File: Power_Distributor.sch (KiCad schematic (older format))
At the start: 1 part, among them J1 Thruster_Off_Switch

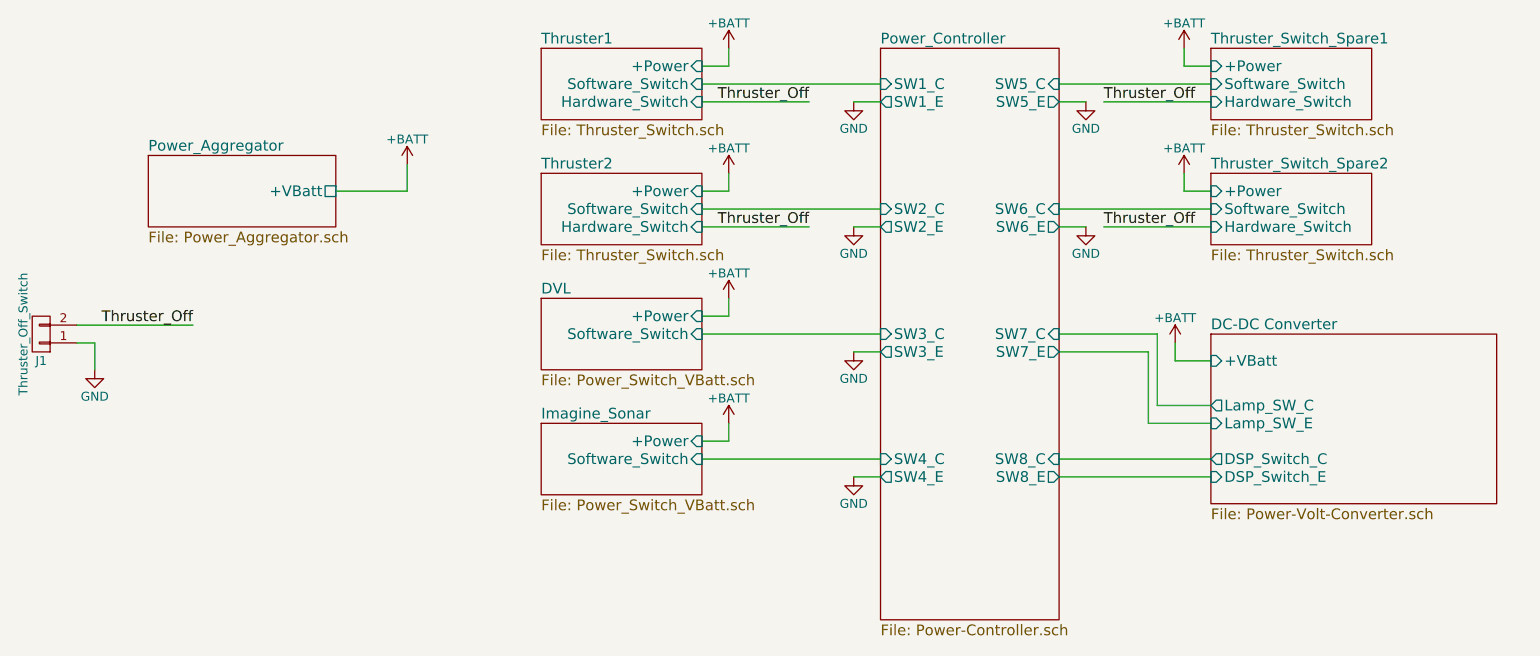
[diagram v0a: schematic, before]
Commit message: Fixed bugs from misunderstanding about Thruster, DVL, and Sonar switch biases.
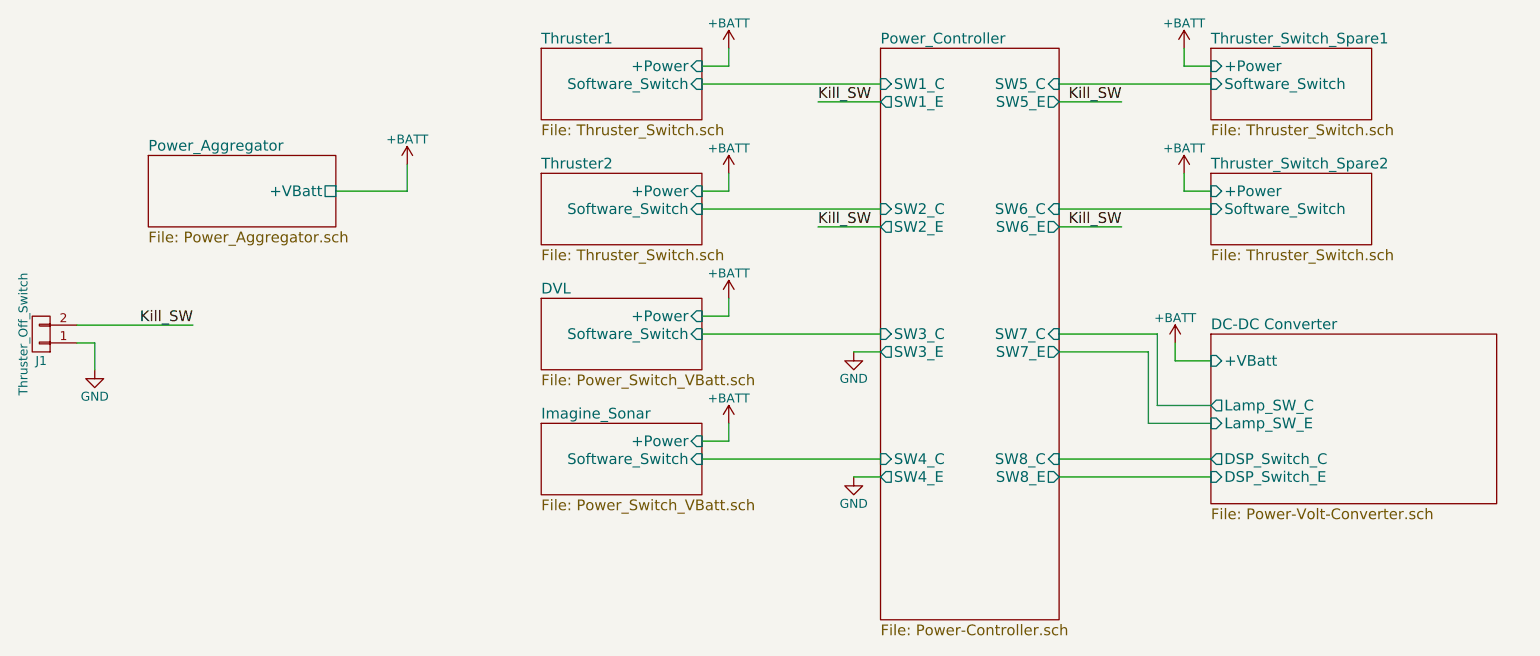
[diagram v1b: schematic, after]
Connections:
- net Thruster_Off renamed Kill_SW
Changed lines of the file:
@@
 F2 "+Power" I R 5450 3350 60
 F3 "Software_Switch" I R 5450 3450 60
-F4 "Hardware_Switch" I R 5450 3550 60
 $EndSheet
 $Sheet
@@
 F2 "+Power" I L 8300 2650 60
 F3 "Software_Switch" I L 8300 2750 60
-F4 "Hardware_Switch" I L 8300 2850 60
 $EndSheet
 $Sheet
@@
 F2 "+Power" I L 8300 3350 60
 F3 "Software_Switch" I L 8300 3450 60
-F4 "Hardware_Switch" I L 8300 3550 60
 $EndSheet
 $Comp
@@
 $EndComp
 Text Label 2600 4100 2    60   ~ 0
-Thruster_Off
+Kill_SW
 $Comp
 L GND #PWR1
@@
 	1    0    0    -1
 $EndComp
-Text Label 6050 2850 2    60   ~ 0
-Thruster_Off
 $Sheet
 S 4550 2550 900  400
@@
 F2 "+Power" I R 5450 2650 60
 F3 "Software_Switch" I R 5450 2750 60
-F4 "Hardware_Switch" I R 5450 2850 60
-$EndSheet
-Text Label 6050 3550 2    60   ~ 0
-Thruster_Off
+$EndSheet
 Wire Wire Line
 	1950 4200 2050 4200
@@
 Wire Wire Line
 	2600 4100 1950 4100
-Text Label 7700 2850 0    60   ~ 0
-Thruster_Off
-Wire Wire Line
-	7700 2850 8300 2850
-Wire Wire Line
-	6050 2850 5450 2850
-Wire Wire Line
-	6050 3550 5450 3550
-Text Label 7700 3550 0    60   ~ 0
-Thruster_Off
-Wire Wire Line
-	7700 3550 8300 3550
 $Comp
 L +BATT #PWR3
@@
 	5600 4750 5600 4650
 $Comp
-L +BATT #PWR14
+L +BATT #PWR10
 U 1 1 58EC0437
 P 8150 2550
-F 0 "#PWR14" H 8150 2400 50  0001 C CNN
+F 0 "#PWR10" H 8150 2400 50  0001 C CNN
 F 1 "+BATT" H 8150 2690 50  0000 C CNN
 F 2 "" H 8150 2550 50  0001 C CNN
@@
 	8150 2650 8300 2650
 $Comp
-L +BATT #PWR15
+L +BATT #PWR11
 U 1 1 58ECB208
 P 8150 3250
-F 0 "#PWR15" H 8150 3100 50  0001 C CNN
+F 0 "#PWR11" H 8150 3100 50  0001 C CNN
 F 1 "+BATT" H 8150 3390 50  0000 C CNN
 F 2 "" H 8150 3250 50  0001 C CNN
@@
 $EndSheet
 $Comp
-L +BATT #PWR13
+L +BATT #PWR9
 U 1 1 58E67F6C
 P 8100 4200
-F 0 "#PWR13" H 8100 4050 50  0001 C CNN
+F 0 "#PWR9" H 8100 4050 50  0001 C CNN
 F 1 "+BATT" H 8100 4340 50  0000 C CNN
 F 2 "" H 8100 4200 50  0001 C CNN
@@
 $Comp
 L GND #PWR7
-U 1 1 58E667A4
-P 6300 2850
-F 0 "#PWR7" H 6300 2600 50  0001 C CNN
-F 1 "GND" H 6300 2700 50  0000 C CNN
-F 2 "" H 6300 2850 50  0001 C CNN
-F 3 "" H 6300 2850 50  0001 C CNN
-	1    6300 2850
-	1    0    0    -1
-$EndComp
-$Comp
-L GND #PWR8
-U 1 1 58E66896
-P 6300 3550
-F 0 "#PWR8" H 6300 3300 50  0001 C CNN
-F 1 "GND" H 6300 3400 50  0000 C CNN
-F 2 "" H 6300 3550 50  0001 C CNN
-F 3 "" H 6300 3550 50  0001 C CNN
-	1    6300 3550
-	1    0    0    -1
-$EndComp
-$Comp
-L GND #PWR9
 U 1 1 58E66A79
 P 6300 4250
-F 0 "#PWR9" H 6300 4000 50  0001 C CNN
+F 0 "#PWR7" H 6300 4000 50  0001 C CNN
 F 1 "GND" H 6300 4100 50  0000 C CNN
 F 2 "" H 6300 4250 50  0001 C CNN
@@
 $EndComp
 $Comp
-L GND #PWR10
+L GND #PWR8
 U 1 1 58E66B6B
 P 6300 4950
-F 0 "#PWR10" H 6300 4700 50  0001 C CNN
+F 0 "#PWR8" H 6300 4700 50  0001 C CNN
 F 1 "GND" H 6300 4800 50  0000 C CNN
 F 2 "" H 6300 4950 50  0001 C CNN
@@
 	1    0    0    -1
 $EndComp
-$Comp
-L GND #PWR12
-U 1 1 58E66C5D
-P 7600 3550
-F 0 "#PWR12" H 7600 3300 50  0001 C CNN
-F 1 "GND" H 7600 3400 50  0000 C CNN
-F 2 "" H 7600 3550 50  0001 C CNN
-F 3 "" H 7600 3550 50  0001 C CNN
-	1    7600 3550
-	1    0    0    -1
-$EndComp
-$Comp
-L GND #PWR11
-U 1 1 58E66D4F
-P 7600 2850
-F 0 "#PWR11" H 7600 2600 50  0001 C CNN
-F 1 "GND" H 7600 2700 50  0000 C CNN
-F 2 "" H 7600 2850 50  0001 C CNN
-F 3 "" H 7600 2850 50  0001 C CNN
-	1    7600 2850
-	1    0    0    -1
-$EndComp
-Wire Wire Line
-	6450 2850 6300 2850
-Wire Wire Line
-	6450 3550 6300 3550
+Wire Wire Line
+	6100 2850 6450 2850
+Wire Wire Line
+	6100 3550 6450 3550
 Wire Wire Line
 	6300 4250 6450 4250
@@
 	6450 4950 6300 4950
 Wire Wire Line
-	7450 3550 7600 3550
-Wire Wire Line
-	7450 2850 7600 2850
+	7450 3550 7800 3550
+Wire Wire Line
+	7450 2850 7800 2850
+Text Label 6100 2850 0    60   ~ 0
+Kill_SW
+Text Label 6100 3550 0    60   ~ 0
+Kill_SW
+Text Label 7800 2850 2    60   ~ 0
+Kill_SW
+Text Label 7800 3550 2    60   ~ 0
+Kill_SW
 $EndSCHEMATC

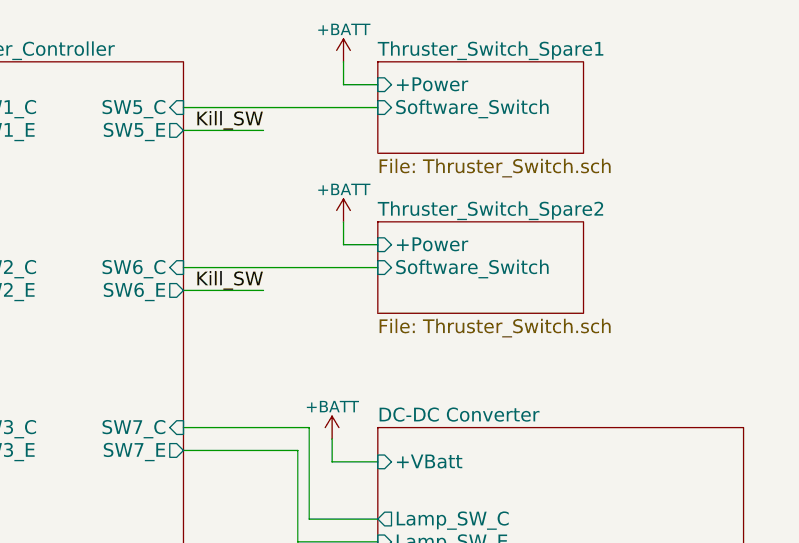
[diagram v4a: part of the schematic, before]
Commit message: Ver1 Power_dist PCB
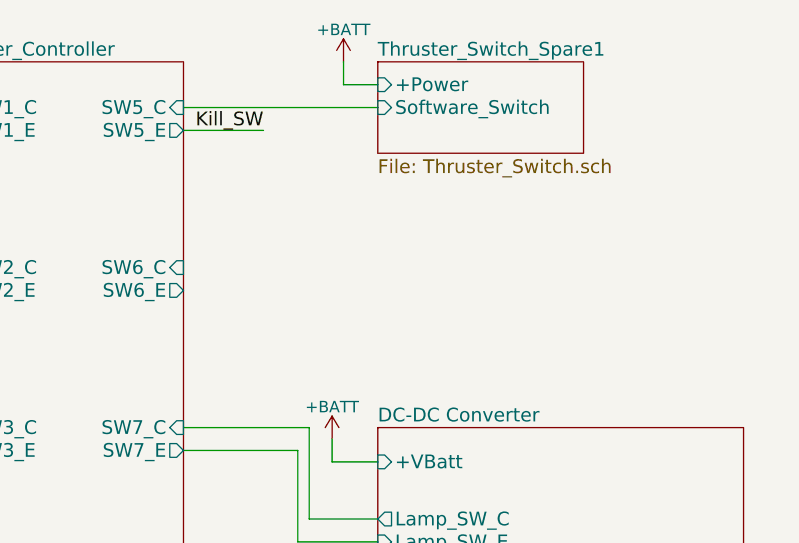
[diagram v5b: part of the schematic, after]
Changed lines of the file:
@@
 $Descr A4 11693 8268
 encoding utf-8
-Sheet 1 10
+Sheet 1 9
 Title "Power Distributor"
 Date "2017-04-06"
@@
 F3 "Software_Switch" I L 8300 2750 60
 $EndSheet
-$Sheet
-S 8300 3250 900  400
-U 58E6D43E
-F0 "Thruster_Switch_Spare2" 60
-F1 "Thruster_Switch.sch" 60
-F2 "+Power" I L 8300 3350 60
-F3 "Software_Switch" I L 8300 3450 60
-$EndSheet
 $Comp
 L +BATT #PWR2
@@
 Wire Wire Line
 	8150 2650 8300 2650
-$Comp
-L +BATT #PWR11
-U 1 1 58ECB208
-P 8150 3250
-F 0 "#PWR11" H 8150 3100 50  0001 C CNN
-F 1 "+BATT" H 8150 3390 50  0000 C CNN
-F 2 "" H 8150 3250 50  0001 C CNN
-F 3 "" H 8150 3250 50  0001 C CNN
-	1    8150 3250
-	1    0    0    -1
-$EndComp
-Wire Wire Line
-	8150 3250 8150 3350
-Wire Wire Line
-	8150 3350 8300 3350
 $Sheet
 S 6450 2550 1000 3200
@@
 Wire Wire Line
 	7450 2750 8300 2750
-Wire Wire Line
-	7450 3450 8300 3450
 $Comp
 L GND #PWR7
@@
 	6450 4950 6300 4950
 Wire Wire Line
-	7450 3550 7800 3550
-Wire Wire Line
 	7450 2850 7800 2850
 Text Label 6100 2850 0    60   ~ 0
@@
 Text Label 7800 2850 2    60   ~ 0
 Kill_SW
-Text Label 7800 3550 2    60   ~ 0
-Kill_SW
 $EndSCHEMATC

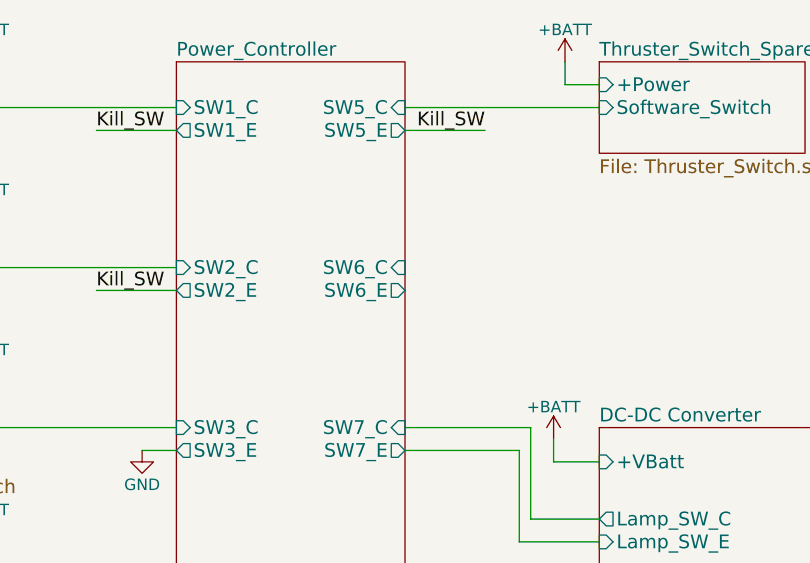
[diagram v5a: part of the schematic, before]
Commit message: Correct GND mixed-up and re-route USB signals as a differential pairs with match length.
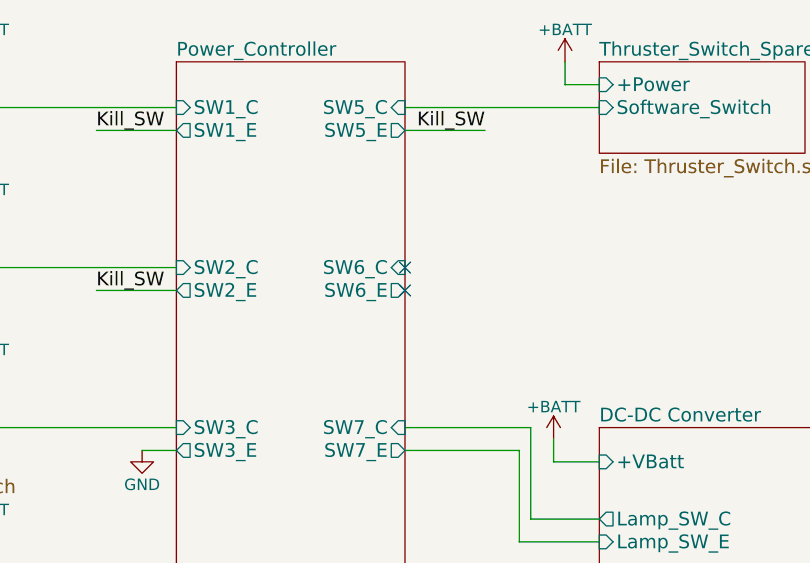
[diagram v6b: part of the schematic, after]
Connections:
- no-connect marks 0 -> 2
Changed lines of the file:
@@
 $EndSheet
 $Comp
-L +BATT #PWR2
+L +BATT #PWR01
 U 1 1 58E61C00
 P 3800 3200
-F 0 "#PWR2" H 3800 3050 50  0001 C CNN
+F 0 "#PWR01" H 3800 3050 50  0001 C CNN
 F 1 "+BATT" H 3800 3340 50  0000 C CNN
 F 2 "" H 3800 3200 50  0001 C CNN
@@
 Kill_SW
 $Comp
-L GND #PWR1
+L GND #PWR02
 U 1 1 58E6E6F3
 P 2050 4350
-F 0 "#PWR1" H 2050 4100 50  0001 C CNN
+F 0 "#PWR02" H 2050 4100 50  0001 C CNN
 F 1 "GND" H 2050 4200 50  0000 C CNN
 F 2 "" H 2050 4350 50  0001 C CNN
@@
 	2600 4100 1950 4100
 $Comp
-L +BATT #PWR3
+L +BATT #PWR03
 U 1 1 58EB597A
 P 5600 2550
-F 0 "#PWR3" H 5600 2400 50  0001 C CNN
+F 0 "#PWR03" H 5600 2400 50  0001 C CNN
 F 1 "+BATT" H 5600 2690 50  0000 C CNN
 F 2 "" H 5600 2550 50  0001 C CNN
@@
 	5600 2650 5450 2650
 $Comp
-L +BATT #PWR4
+L +BATT #PWR04
 U 1 1 58EB69B2
 P 5600 3250
-F 0 "#PWR4" H 5600 3100 50  0001 C CNN
+F 0 "#PWR04" H 5600 3100 50  0001 C CNN
 F 1 "+BATT" H 5600 3390 50  0000 C CNN
 F 2 "" H 5600 3250 50  0001 C CNN
@@
 	5600 3350 5450 3350
 $Comp
-L +BATT #PWR5
+L +BATT #PWR05
 U 1 1 58EB9A19
 P 5600 3950
-F 0 "#PWR5" H 5600 3800 50  0001 C CNN
+F 0 "#PWR05" H 5600 3800 50  0001 C CNN
 F 1 "+BATT" H 5600 4090 50  0000 C CNN
 F 2 "" H 5600 3950 50  0001 C CNN
@@
 	5600 4050 5450 4050
 $Comp
-L +BATT #PWR6
+L +BATT #PWR06
 U 1 1 58EBAA49
 P 5600 4650
-F 0 "#PWR6" H 5600 4500 50  0001 C CNN
+F 0 "#PWR06" H 5600 4500 50  0001 C CNN
 F 1 "+BATT" H 5600 4790 50  0000 C CNN
 F 2 "" H 5600 4650 50  0001 C CNN
@@
 	5600 4750 5600 4650
 $Comp
-L +BATT #PWR10
+L +BATT #PWR07
 U 1 1 58EC0437
 P 8150 2550
-F 0 "#PWR10" H 8150 2400 50  0001 C CNN
+F 0 "#PWR07" H 8150 2400 50  0001 C CNN
 F 1 "+BATT" H 8150 2690 50  0000 C CNN
 F 2 "" H 8150 2550 50  0001 C CNN
@@
 $EndSheet
 $Comp
-L +BATT #PWR9
+L +BATT #PWR08
 U 1 1 58E67F6C
 P 8100 4200
-F 0 "#PWR9" H 8100 4050 50  0001 C CNN
+F 0 "#PWR08" H 8100 4050 50  0001 C CNN
 F 1 "+BATT" H 8100 4340 50  0000 C CNN
 F 2 "" H 8100 4200 50  0001 C CNN
@@
 	7450 2750 8300 2750
 $Comp
-L GND #PWR7
+L GND #PWR09
 U 1 1 58E66A79
 P 6300 4250
-F 0 "#PWR7" H 6300 4000 50  0001 C CNN
+F 0 "#PWR09" H 6300 4000 50  0001 C CNN
 F 1 "GND" H 6300 4100 50  0000 C CNN
 F 2 "" H 6300 4250 50  0001 C CNN
@@
 $EndComp
 $Comp
-L GND #PWR8
+L GND #PWR010
 U 1 1 58E66B6B
 P 6300 4950
-F 0 "#PWR8" H 6300 4700 50  0001 C CNN
+F 0 "#PWR010" H 6300 4700 50  0001 C CNN
 F 1 "GND" H 6300 4800 50  0000 C CNN
 F 2 "" H 6300 4950 50  0001 C CNN
@@
 Text Label 7800 2850 2    60   ~ 0
 Kill_SW
+NoConn ~ 7450 3450
+NoConn ~ 7450 3550
 $EndSCHEMATC
